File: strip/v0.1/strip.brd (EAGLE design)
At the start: 100 x 11 mm, 101 parts, among them IC1 LP2992, IC11 AP1115BY50, IC2 ADP3110A-SO8, IC3 STM32-M-48, IC4 OPA335, IC5 ADP3110A-SO8, IC6 ADP3110A-SO8, Q1 IRF7828, Q2 IRF7828, Q3 IRF7828, Q4 IRF7828, Q5 IRF7828, Q6 IRF7828

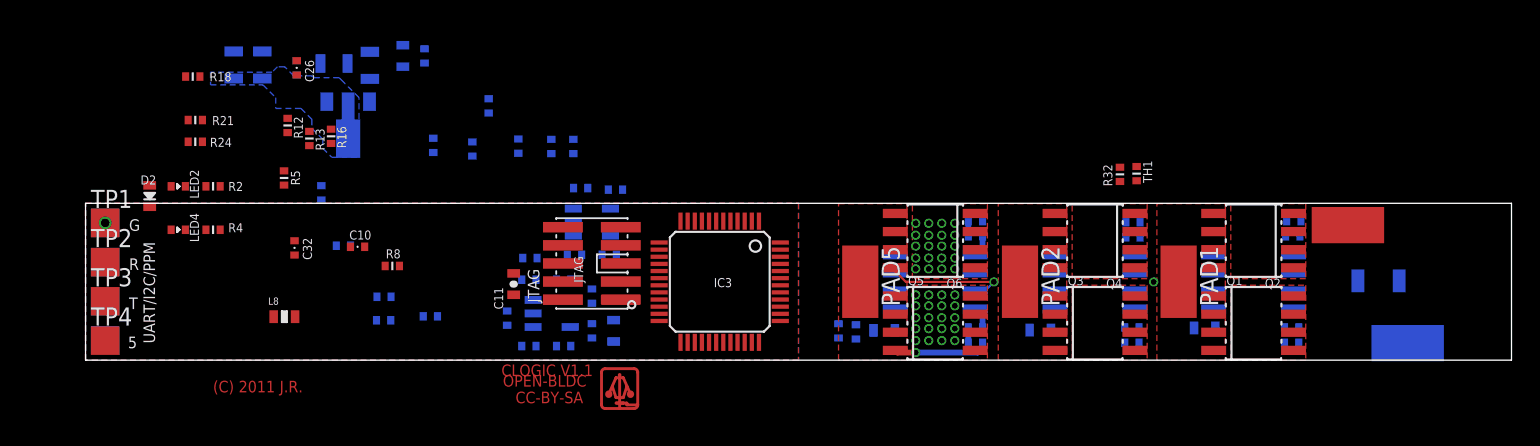
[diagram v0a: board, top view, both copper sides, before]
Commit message: More work on strip. Preliminary routing of the power stage.
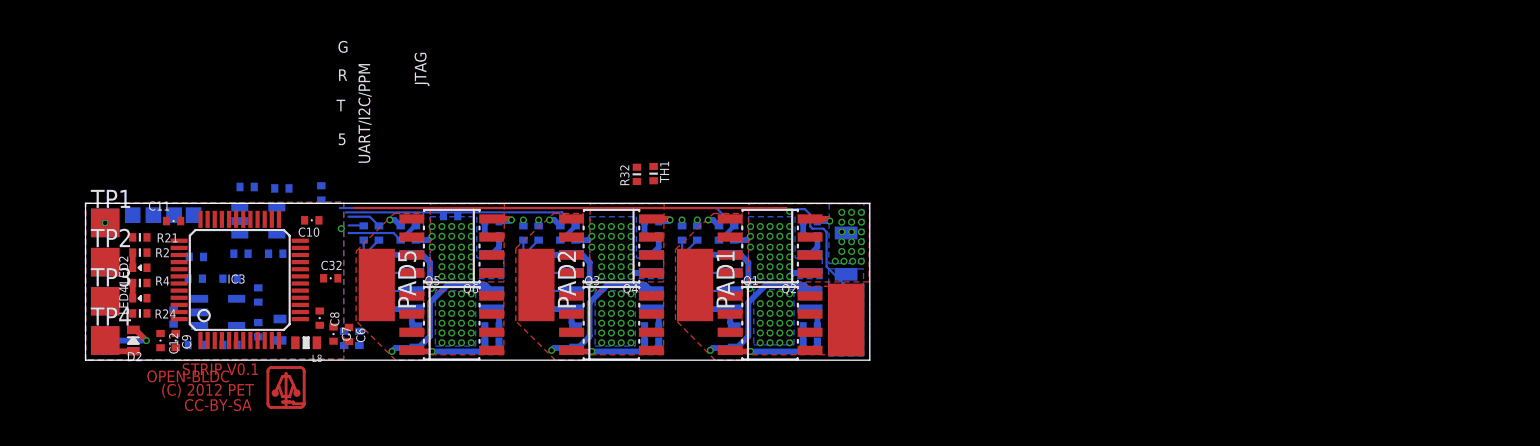
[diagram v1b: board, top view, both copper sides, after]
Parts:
- removed C14, C15, C17, C18: 22u, pel_dipol_comp:0805-POL-CAP
- removed C33: 100n, pel_dipol_comp:0402-CAP
- removed D5: CDBU0130, pel_dipol_comp:0603-LED
- removed DRILEGEND: (no value), drilegend:DRILEGEND
- removed IC11: AP1115BY50, clogic-v0_3-r1:SOT89
- removed JTAG: CONN_5-2-FTSH-V, pel_misc:FTSH-105-DV
- added TP10, TP11, TP12, TP13: TPSQTP11SQ, testpad:TP11SQ
- C11: device pel_dipol_comp:0603-CAP -> pel_dipol_comp:0402-CAP
- moved PAD3 39.4 mm to (53.3, 2.82), flipped to the top, turned to 180 degrees
- moved R18 38.5 mm to (44.4, 8.92), flipped to the bottom, turned to 270 degrees
- moved R45 37.4 mm to (53.3, 7.47), turned to 270 degrees
- moved PAD4 35.8 mm to (53.3, 2.82), flipped to the bottom, turned to 0 degrees
- moved Q2 33.9 mm to (48.0, 8.00)
- moved Q4 33.9 mm to (36.9, 8.00)
- moved Q6 33.9 mm to (25.7, 8.00)
- moved PAD1 33.9 mm to (42.7, 5.27)
- moved PAD2 33.9 mm to (31.6, 5.27)
- moved PAD5 33.9 mm to (20.4, 5.27)
- moved L6 33.9 mm to (28.5, 2.36)
- moved R50 33.9 mm to (28.5, 1.30)
- moved IC6 33.9 mm to (48.0, 5.49)
- moved L7 33.9 mm to (28.5, 8.69)
- moved Q1 33.9 mm to (48.0, 2.59)
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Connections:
- removed net +5V: C1.P$1, C2.P$1, D2.C, D5.C, IC1.1, IC1.3, LED2.A, LED4.A, TP8.TP
- removed net +5VOUT: C14.+, C15.+, D5.A, IC11.P$3
- removed net PS_GND: IC2.6, IC5.6, IC6.6, Q2.1, Q2.2, Q2.3, Q4.1, Q4.2, Q4.3, Q6.1, Q6.2, Q6.3, R27.P$2, R45.P$1
- new net SHUNT: PAD4.1, R27.P$2, R45.P$2
- net +3V3: now also LED2.A, LED4.A; no longer JTAG.1
- net BUSS+: now also C1.P$1, C2.P$1, D2.C, IC1.1, IC1.3, TP8.TP; no longer C17.+, C18.+, C33.P$1, IC11.P$2, IC11.P$4
- net CAN_RX: now also IC3.45; no longer IC3.32
- net CAN_TX: now also IC3.46; no longer IC3.33
- net GND: now also IC2.6, IC5.6, IC6.6, Q2.1, Q2.2, Q2.3, Q4.1, Q4.2, Q4.3, Q6.1, Q6.2, Q6.3, R45.P$1, TP10.TP; no longer C14.-, C15.-, C17.-, C18.-, C33.P$2, IC11.P$1, JTAG.3, JTAG.5, JTAG.7, JTAG.9, PAD4.1, R45.P$2
- net LEDG: now also IC3.40; no longer IC3.16
- net LEDR: now also IC3.41; no longer IC3.17
- net RST: no longer JTAG.10
- net TCK/SWCLK: now also TP12.TP; no longer JTAG.4
- net TDI: no longer JTAG.8
- net TDO/TRACESWO: now also TP13.TP; no longer JTAG.6
- net TMS/SWDIO: now also TP11.TP; no longer JTAG.2
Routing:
- net SHUNT: track 0.00 -> 41.2 mm, vias 0 -> 1
- net W_VOLTAGE: track 0.00 -> 29.7 mm
- net N$39: track 0.00 -> 25.3 mm, vias 0 -> 1
- net N$45: track 0.00 -> 24.6 mm, vias 0 -> 1
- net BUSS+: track 0.00 -> 20.8 mm, vias 20 -> 73
- net V_VOLTAGE: track 0.00 -> 18.0 mm
- net N$42: track 0.00 -> 12.8 mm, vias 0 -> 1
- net N$36: track 0.00 -> 11.5 mm, vias 0 -> 1
- net PHASE_V: track 0.00 -> 11.4 mm, vias 0 -> 2
- net PHASE_W: track 0.00 -> 11.4 mm, vias 0 -> 2
- net GND: track 0.00 -> 8.98 mm, vias 21 -> 102
- net N$31: track 0.00 -> 6.59 mm, vias 0 -> 1
- net N$29: track 0.00 -> 6.59 mm, vias 0 -> 1
- net V_PWM: track 0.00 -> 6.07 mm
- net U_PWM: track 0.00 -> 6.07 mm
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- added copper zone on layer 16, net BUSS+
- added copper zone on layer 2, net BUSS+
- added copper zone on layer 15, net GND
- added copper zone on layer 16, net SHUNT
- removed copper zone on layer 15, net +12V
- removed copper zone on layer 16, net +12V
- removed copper zone on layer 15, net +5V
- removed copper zone on layer 2, net CAN_GND
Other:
- board size 100 x 11 mm -> 55 x 11 mm
- board text added: "(C) 2012 PET"
- board text added: "STRIP V0.1"
- board text removed: "(C) 2011 J.R."
- board text removed: "CLOGIC V1.0"
- board text removed: "CLOGIC V1.1"

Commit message: Logic is on real GND now not pstage GND, to prevent current related logic signal bouncing. Added mounting holes.
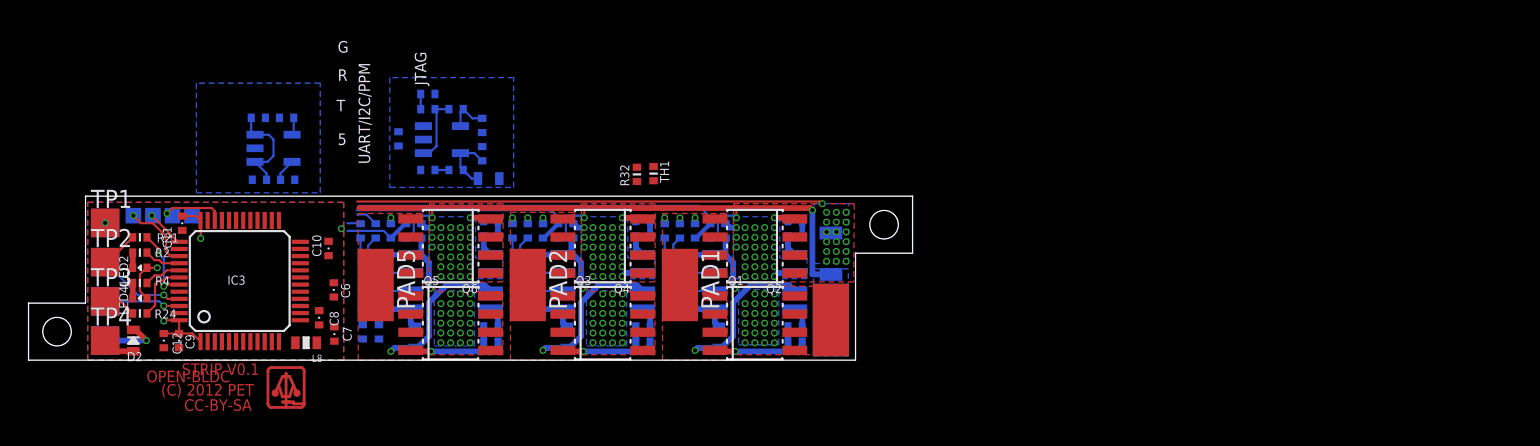
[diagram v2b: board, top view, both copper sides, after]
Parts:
- moved C32 27.9 mm to (44.9, 9.07), flipped to the bottom, turned to 90 degrees
- moved R28 20.4 mm to (24.0, 13.3)
- moved R37 20.2 mm to (24.0, 17.6)
- moved R27 20.1 mm to (21.9, 15.5)
- moved R29 20.0 mm to (26.0, 13.3)
- moved C19 20.0 mm to (27.8, 14.5)
- moved C20 19.9 mm to (24.0, 18.7)
- moved IC4 19.8 mm to (25.0, 15.5)
- moved R31 19.8 mm to (26.0, 17.6)
- moved R30 19.7 mm to (27.8, 16.5)
- moved L1 18.1 mm to (28.3, 12.7), turned to 180 degrees
- moved C27 17.9 mm to (34.2, 9.07), turned to 90 degrees
- moved C2 5.34 mm to (12.2, 12.6)
- moved C4 5.25 mm to (14.2, 12.6)
- moved IC1 5.22 mm to (13.2, 14.9)
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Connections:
- removed net SHUNT: PAD4.1, R27.P$2, R45.P$2
- new net PGND: C26.P$2, C27.P$2, C32.P$2, IC2.6, IC5.6, IC6.6, Q2.1, Q2.2, Q2.3, Q4.1, Q4.2, Q4.3, Q6.1, Q6.2, Q6.3, R27.P$2, R45.P$1
- net GND: now also PAD4.1, R45.P$2; no longer C26.P$2, C27.P$2, C32.P$2, IC2.6, IC5.6, IC6.6, Q2.1, Q2.2, Q2.3, Q4.1, Q4.2, Q4.3, Q6.1, Q6.2, Q6.3, R45.P$1
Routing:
- net GND: track 8.98 -> 51.6 mm, vias 102 -> 6
- net SHUNT: track 41.2 -> 0.00 mm, vias 1 -> 0
- net PGND: track 0.00 -> 40.5 mm, vias 0 -> 100
- net +3V3: track 0.00 -> 12.4 mm, vias 0 -> 3
- net BUSS+: track 20.8 -> 31.4 mm
- net CAN_RX: track 0.00 -> 6.25 mm, vias 0 -> 1
- net CAN_TX: track 0.00 -> 5.32 mm, vias 0 -> 1
- net RXD: track 0.00 -> 5.04 mm, vias 0 -> 2
- net TDO/TRACESWO: track 0.00 -> 5.01 mm, vias 0 -> 1
- net CURRENT_RAW: track 0.00 -> 4.74 mm
- net TMS/SWDIO: track 0.00 -> 4.65 mm, vias 0 -> 1
- net N$9: track 0.00 -> 4.29 mm
- net TXD: track 0.00 -> 4.17 mm
- net N$12: track 0.00 -> 2.86 mm
- net W_VOLTAGE: track 29.7 -> 27.0 mm
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- added copper zone on layer 1, net PGND
- added copper zone on layer 15, net PGND
- added copper zone on layer 16, net PGND
- added copper zone on layer 2, net PGND
- removed copper zone on layer 15, net GND
- removed copper zone on layer 16, net SHUNT
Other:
- board size 55 x 11 mm -> 62 x 11.5 mm

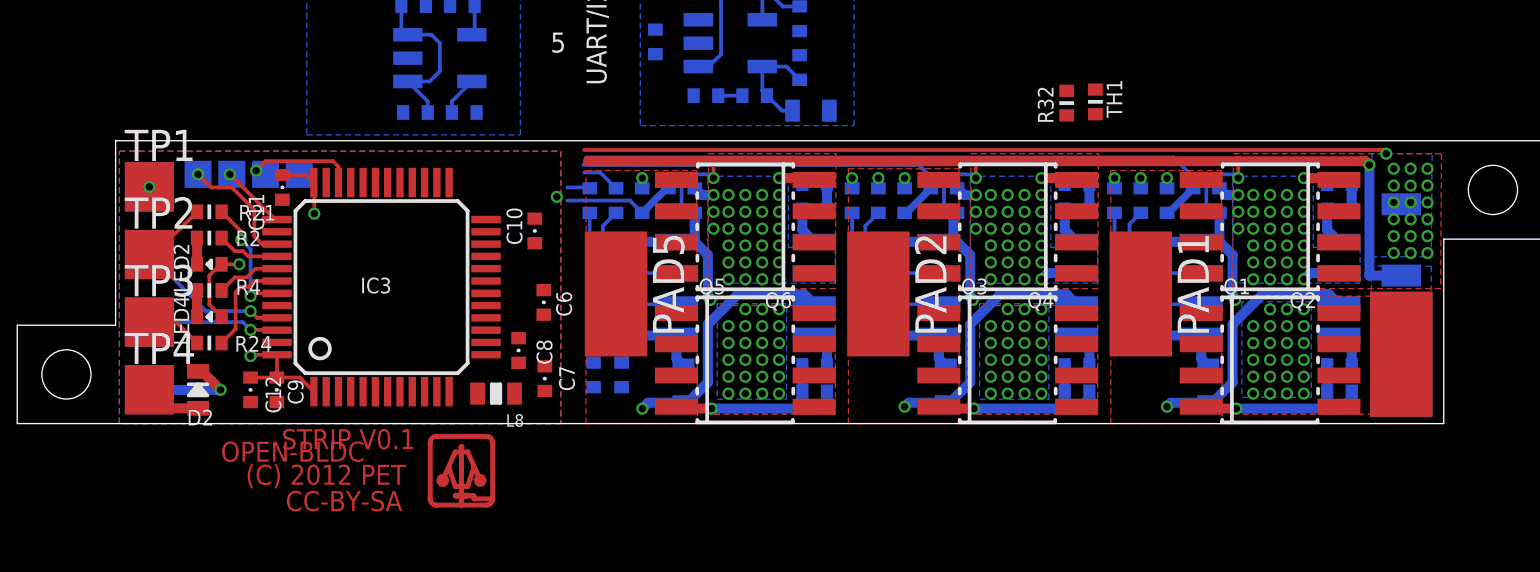
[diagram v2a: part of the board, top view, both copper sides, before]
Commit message: Some more routing on strip. Connected all the control and feedback signals from the powerstage to the MCU.
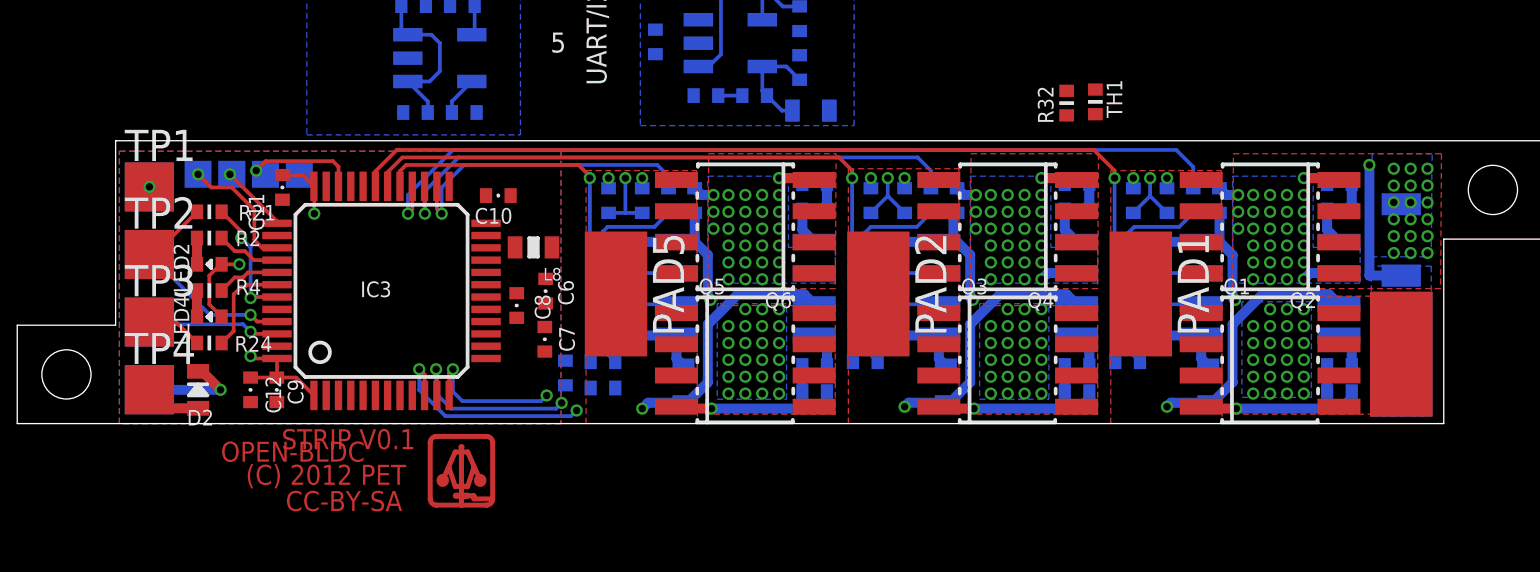
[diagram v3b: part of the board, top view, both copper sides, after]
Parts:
- moved R5 6.57 mm to (19.8, 2.51), turned to 0 degrees
- moved R6 6.57 mm to (30.5, 2.51), turned to 0 degrees
- moved R7 6.57 mm to (41.1, 2.51), turned to 0 degrees
- moved L8 6.14 mm to (17.0, 7.16)
- moved R15 2.44 mm to (20.0, 9.07), turned to 90 degrees
- moved R17 2.44 mm to (30.7, 9.07), turned to 90 degrees
- moved R22 2.44 mm to (41.4, 9.07), turned to 90 degrees
- moved R10 2.13 mm to (43.8, 9.07)
- moved R8 2.13 mm to (22.5, 9.07)
- moved R9 2.13 mm to (33.1, 9.07)
- moved C10 2.07 mm to (15.6, 9.27), turned to 180 degrees
- moved C8 1.83 mm to (16.3, 4.80)
- moved C7 1.60 mm to (17.4, 3.43)
- moved R13 1.15 mm to (18.3, 2.06), turned to 270 degrees
- moved R12 0.93 mm to (19.8, 1.45), turned to 180 degrees
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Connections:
- removed net N$33: IC3.26, R8.P$1
- removed net N$36: IC3.27, R9.P$1
- removed net N$39: IC3.28, R10.P$1
- removed net N$41: IC3.29, R5.P$2
- removed net N$42: IC3.30, R6.P$2
- removed net N$45: IC3.31, R7.P$2
- new net U_!DIS!1: IC2.3, R8.P$2
- new net U_PWM1: IC2.2, R5.P$1
- new net V_!DIS!1: IC5.3, R9.P$2
- new net V_PWM1: IC5.2, R6.P$1
- new net W_!DIS1: IC6.3, R10.P$2
- new net W_PWM1: IC6.2, R7.P$1
- net U_!DIS: now also IC3.26, R8.P$1; no longer IC2.3, R8.P$2
- net U_PWM: now also IC3.29, R5.P$2; no longer IC2.2, R5.P$1
- net V_!DIS: now also IC3.27, R9.P$1; no longer IC5.3, R9.P$2
- net V_PWM: now also IC3.30, R6.P$2; no longer IC5.2, R6.P$1
- net W_!DIS: now also IC3.28, R10.P$1; no longer IC6.3, R10.P$2
- net W_PWM: now also IC3.31, R7.P$2; no longer IC6.2, R7.P$1
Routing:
- net W_PWM: track 6.24 -> 39.2 mm, vias 0 -> 1
- net W_!DIS: track 5.34 -> 35.8 mm, vias 0 -> 1
- net N$39: track 23.3 -> 0.00 mm, vias 1 -> 0
- net N$45: track 22.2 -> 0.00 mm, vias 1 -> 0
- net V_PWM: track 6.29 -> 27.7 mm, vias 0 -> 1
- net U_VOLTAGE: track 4.74 -> 23.8 mm, vias 0 -> 3
- net V_!DIS: track 5.45 -> 24.1 mm, vias 0 -> 1
- net V_VOLTAGE: track 16.3 -> 33.4 mm, vias 0 -> 3
- net W_VOLTAGE: track 27.0 -> 43.1 mm, vias 0 -> 3
- net N$36: track 12.8 -> 0.00 mm, vias 1 -> 0
- net N$42: track 11.5 -> 0.00 mm, vias 1 -> 0
- net U_PWM: track 6.29 -> 16.2 mm, vias 0 -> 1
- net U_!DIS!1: track 0.00 -> 7.45 mm
- net V_!DIS!1: track 0.00 -> 7.43 mm
- net W_!DIS1: track 0.00 -> 7.41 mm
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
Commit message: All airwires routed. Now polishing can begin.
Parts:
- removed R32: 1k, pel_dipol_comp:0402-RES
- removed TH1: 2kOhm, pel_dipol_comp:0402-RES
- moved L1 15.7 mm to (16.1, 2.82), turned to 0 degrees
- moved C3 15.0 mm to (7.85, 3.35), turned to 180 degrees
- moved C1 13.8 mm to (9.83, 3.35), turned to 0 degrees
- moved R29 13.0 mm to (16.8, 4.11)
- moved IC4 13.0 mm to (15.8, 6.25)
- moved R28 13.0 mm to (14.8, 4.11)
- moved C19 13.0 mm to (18.6, 5.26)
- moved R30 13.0 mm to (18.6, 7.24)
- moved R37 13.0 mm to (14.8, 8.46)
- moved R27 12.9 mm to (11.8, 7.62), turned to 0 degrees
- moved C20 12.7 mm to (14.8, 9.98)
- moved R31 12.6 mm to (16.8, 8.99)
- moved IC1 10.4 mm to (8.76, 5.41), turned to 270 degrees
- moved R12 9.49 mm to (11.8, 6.55), turned to 0 degrees
- moved C6 8.88 mm to (9.91, 0.76), flipped to the bottom, turned to 180 degrees
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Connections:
- removed net TEMP: IC3.15, R32.P$2, TH1.P$1
- net +3V3: no longer R32.P$1
- net GND: no longer TH1.P$2
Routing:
- net BUSS+: track 31.4 -> 57.2 mm, vias 73 -> 77
- net PGND: track 43.5 -> 54.5 mm, vias 99 -> 100
- net CURRENT: track 1.07 -> 9.85 mm, vias 0 -> 1
- net N$11: track 0.98 -> 7.63 mm
- net V_BATT: track 0.00 -> 5.84 mm, vias 0 -> 1
- net +3V3: track 12.2 -> 17.8 mm, vias 3 -> 7
- net VDDA: track 0.00 -> 4.52 mm, vias 0 -> 1
- net RST: track 0.00 -> 2.78 mm, vias 0 -> 1
- net GND: track 45.8 -> 47.4 mm, vias 5 -> 13
- net CURRENT_RAW: track 4.74 -> 5.66 mm
- net N$12: track 2.86 -> 3.62 mm

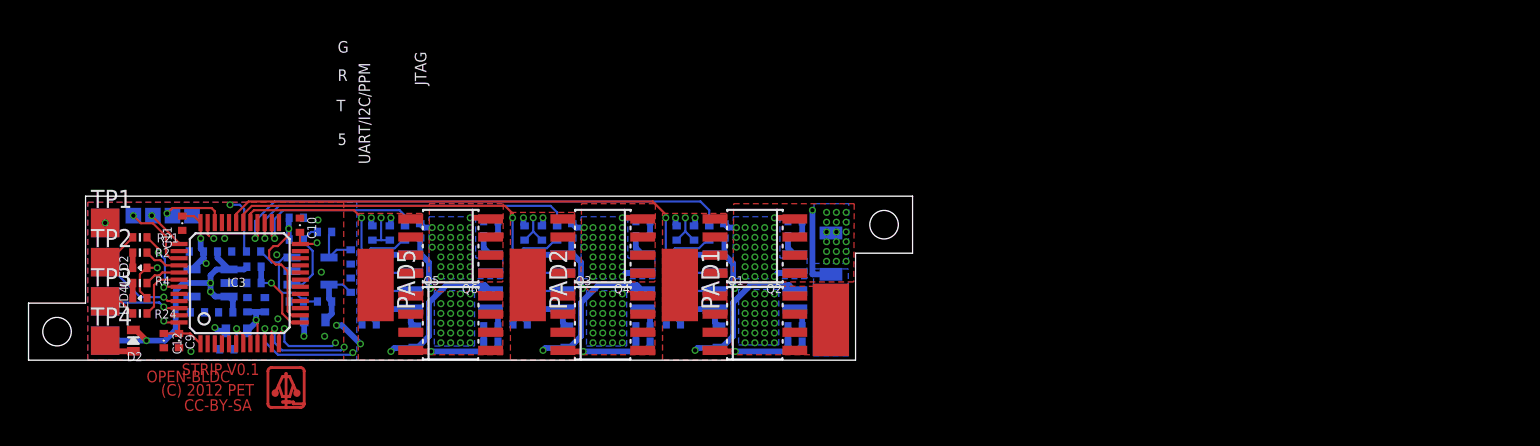
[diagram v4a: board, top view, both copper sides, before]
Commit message: Added power rail tantalum capacitor.
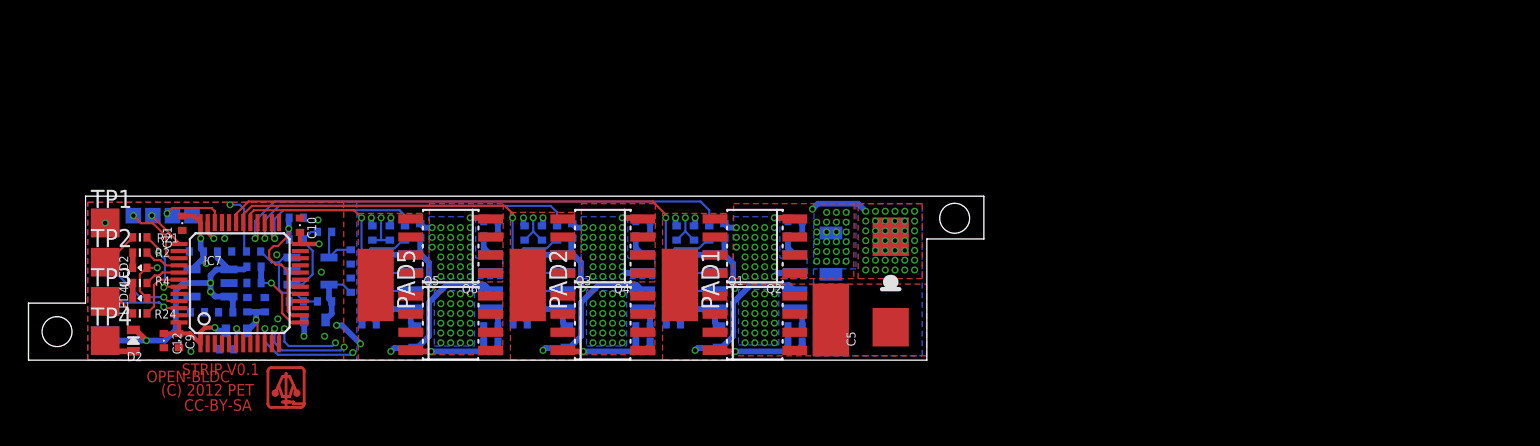
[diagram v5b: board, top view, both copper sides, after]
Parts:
- added C5: (no value), pel_dipol_comp:7343/D
- IC7: value STM32-M-48 -> STM32F050CX
- renumbered IC3 to IC7
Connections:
- net BUSS+: now also C5.+
- net GND: now also C5.-
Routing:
- net GND: track 47.4 -> 45.9 mm, vias 13 -> 55
- net +3V3: track 17.8 -> 18.7 mm, vias 7 -> 6
- net PGND: vias 100 -> 105
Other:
- board size 62 x 11.5 mm -> 67 x 11.5 mm
- board text removed: "5"
- board text removed: "CAN"
- board text removed: "G"
- board text removed: "JTAG"
- board text removed: "R"
- board text removed: "T"
- board text removed: "UART/I2C/PPM"
